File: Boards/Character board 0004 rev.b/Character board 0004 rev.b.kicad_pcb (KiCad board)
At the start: 2 copper layers, 166.4 x 186.7 mm, 64 parts, among them J1 card edge, J2 character connector, Q1 2N6125, U1 2.2K, U10 Unused DIP, U11 ULN2003A, U12 ULN2003A, U13 7406, U14 74LS42, U15 LM741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

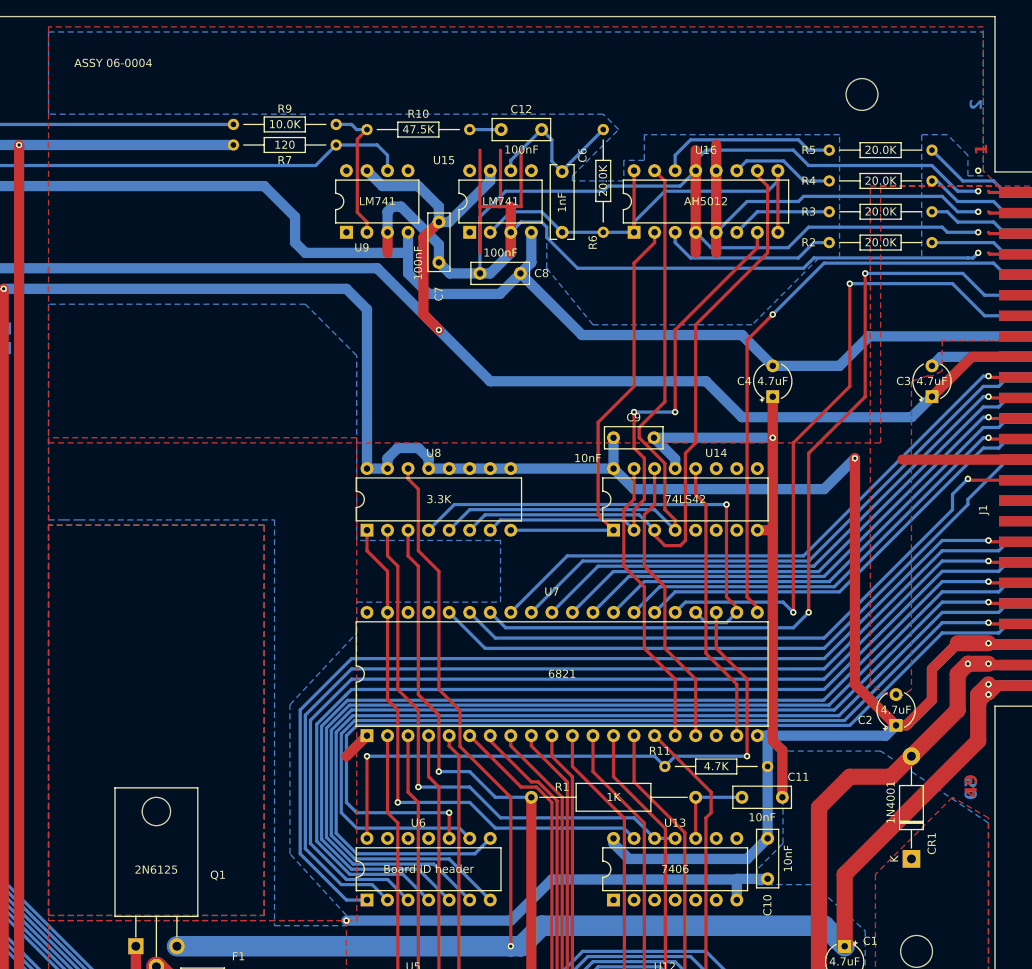
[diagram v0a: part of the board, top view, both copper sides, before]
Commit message: updated boards to have correct logos
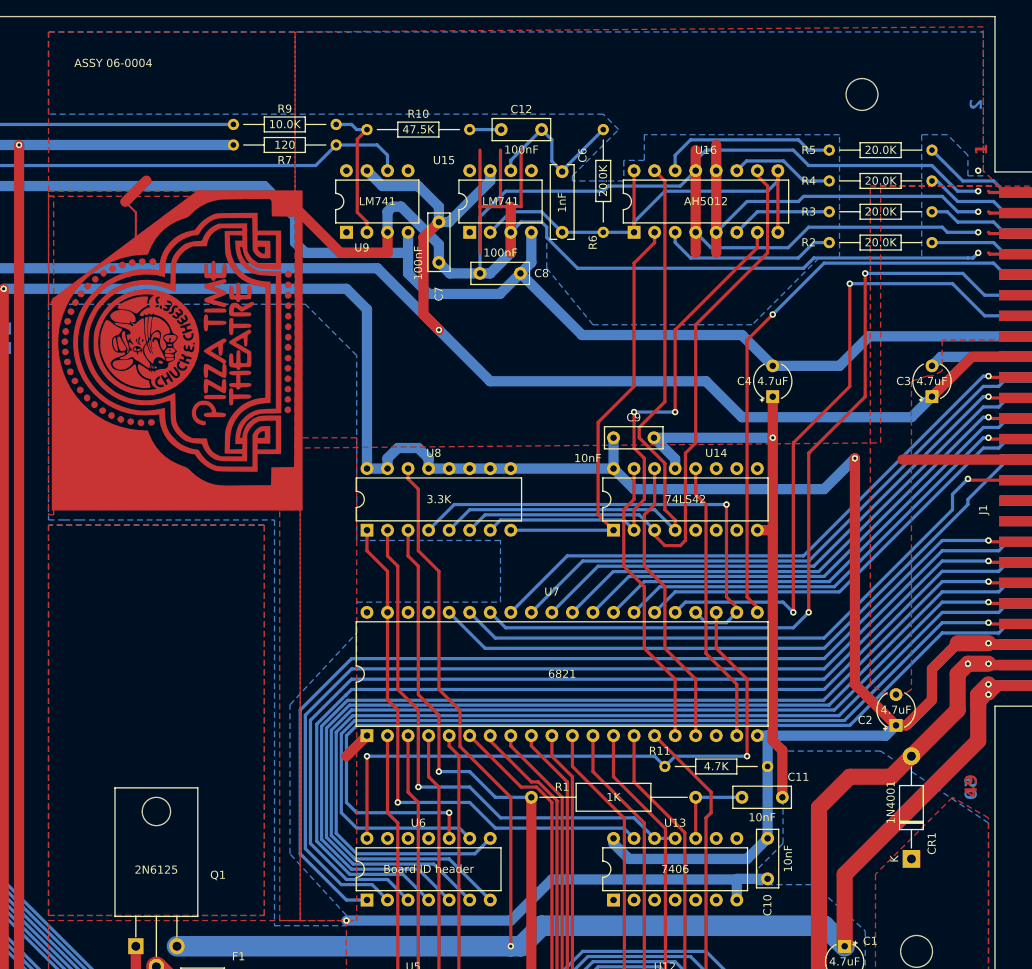
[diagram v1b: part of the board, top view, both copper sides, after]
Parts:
- added G***: LOGO, Evan's parts:PTT white, F.Cu at (83.2, 41.3)
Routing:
- net GND: track 558.6 -> 581.6 mm

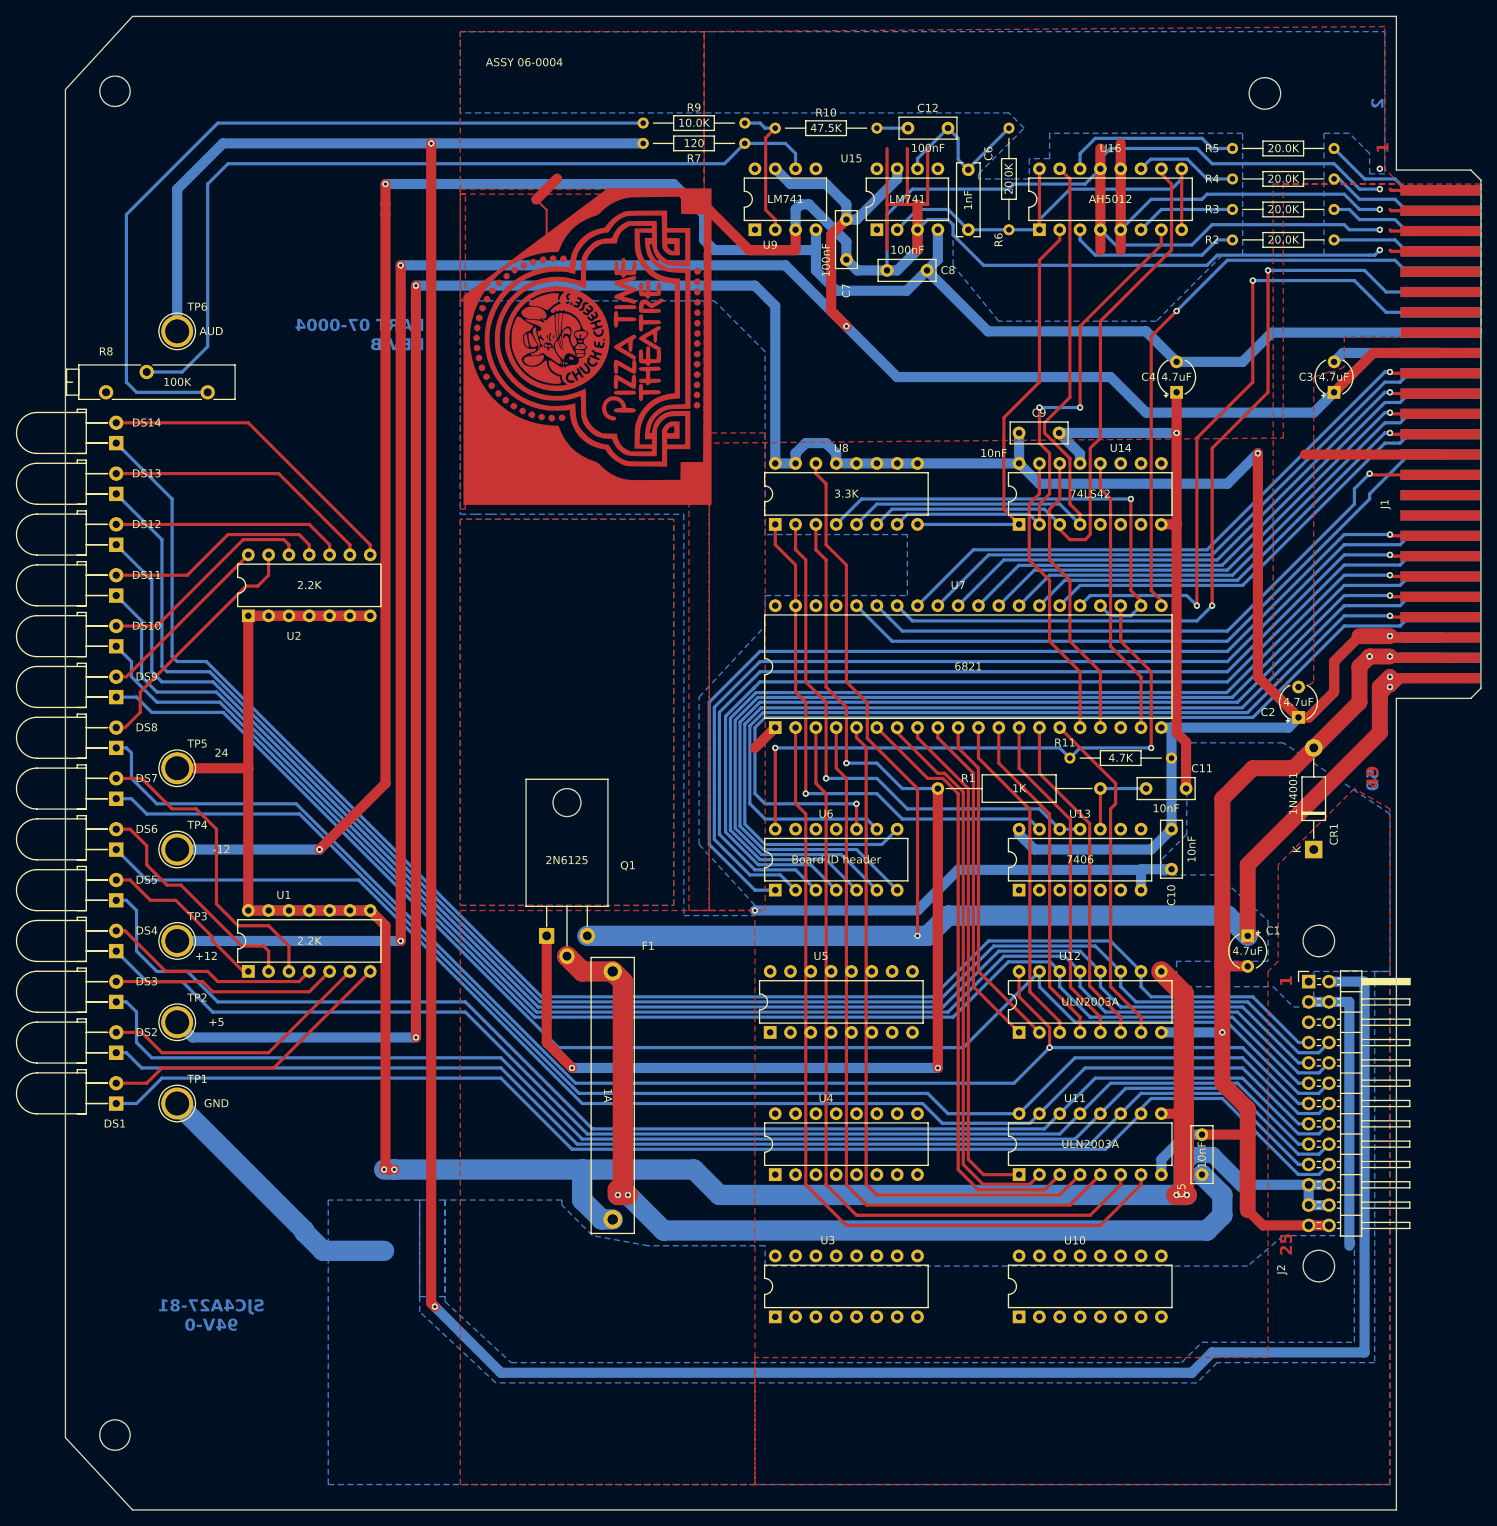
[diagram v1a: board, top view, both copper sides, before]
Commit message: revised LED spacing
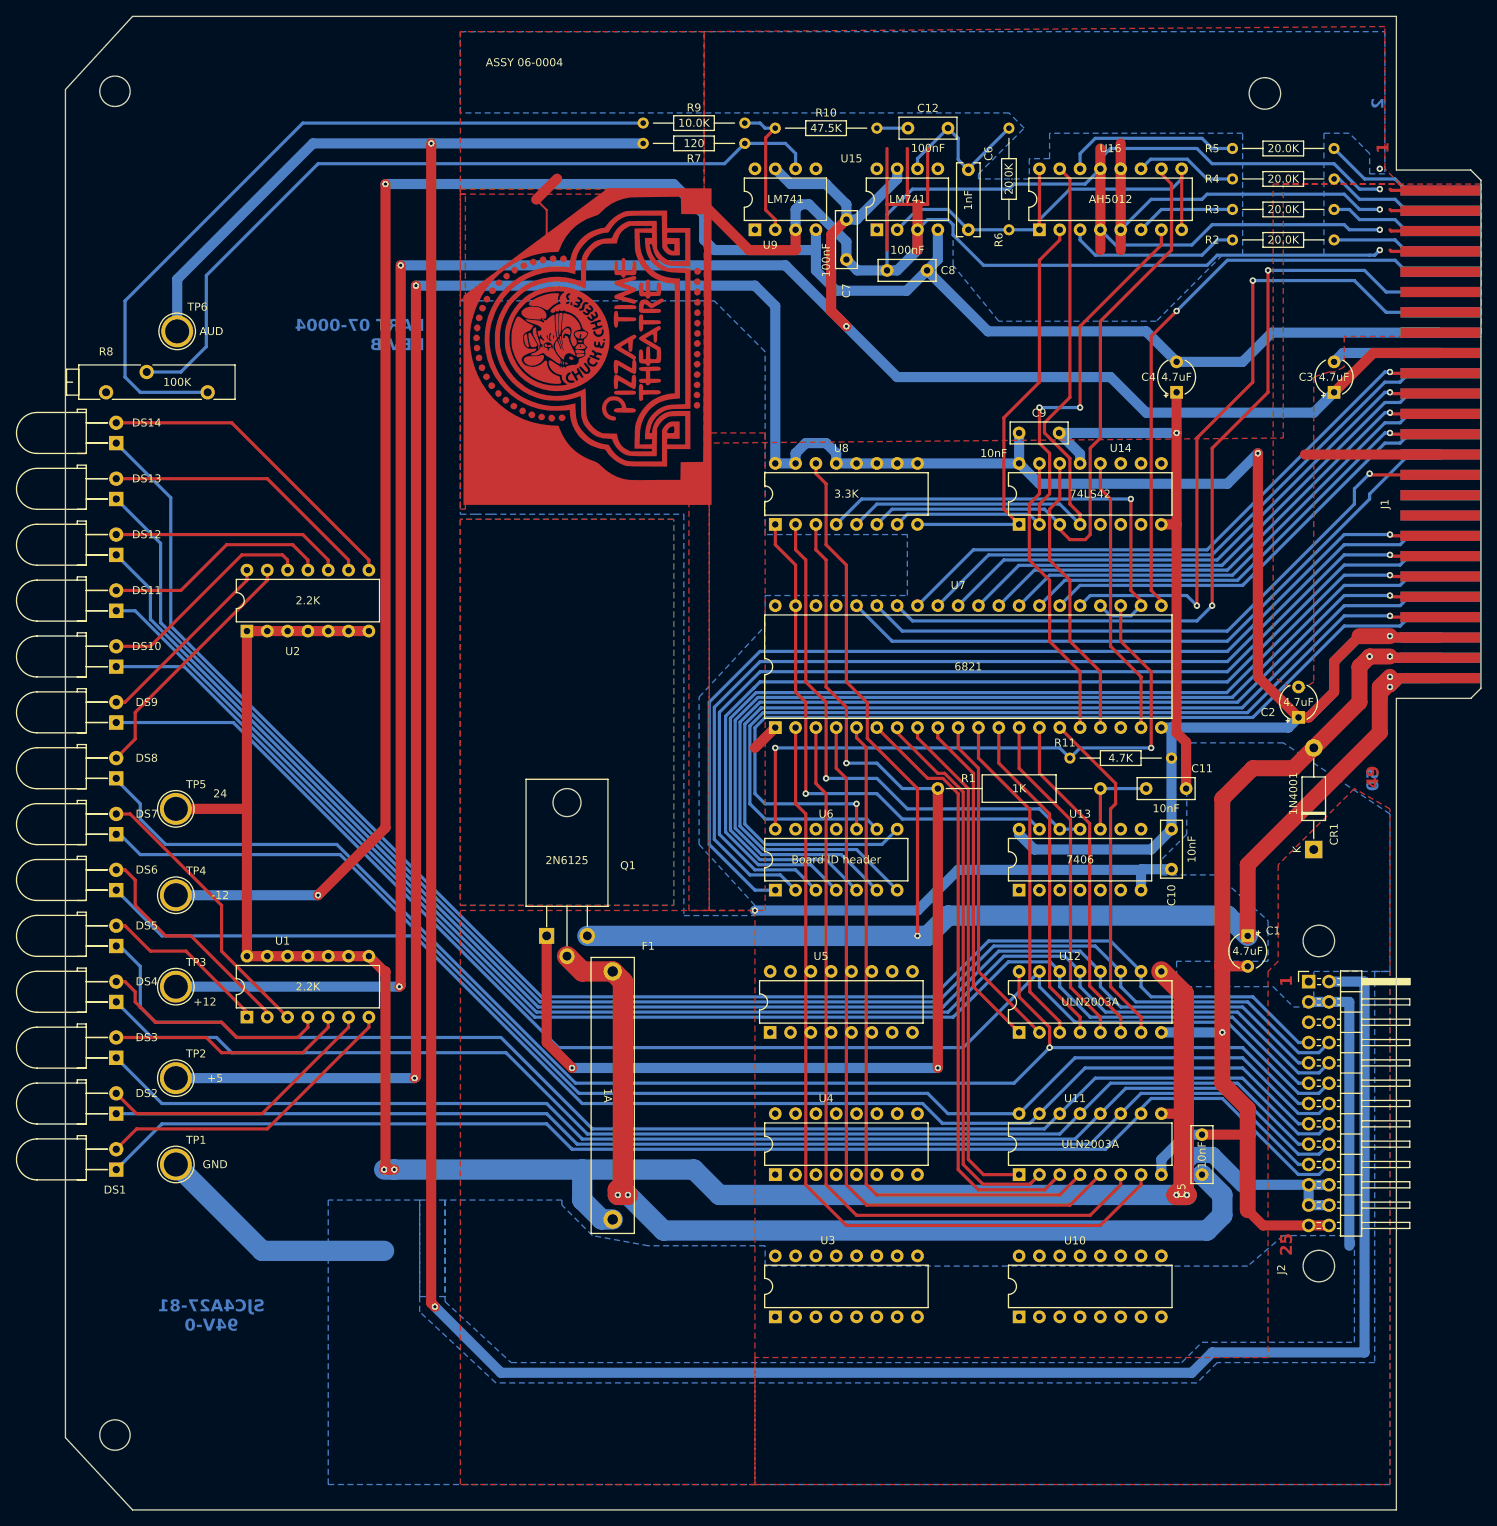
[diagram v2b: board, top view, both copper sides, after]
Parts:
- moved DS1 8.25 mm to (24.3, 141.6)
- moved TP1 7.62 mm to (31.8, 143.5)
- moved DS2 7.62 mm to (24.3, 134.6)
- moved TP2 6.99 mm to (31.8, 132.7)
- moved DS3 6.98 mm to (24.3, 127.6)
- moved DS4 6.35 mm to (24.3, 120.7)
- moved TP3 5.72 mm to (31.8, 121.3)
- moved TP4 5.72 mm to (31.8, 109.9)
- moved U1 5.72 mm to (40.6, 125.1)
- moved DS5 5.72 mm to (24.3, 113.7)
- moved TP5 5.08 mm to (31.8, 99.1)
- moved DS6 5.08 mm to (24.3, 106.7)
- moved DS7 4.44 mm to (24.3, 99.7)
- moved DS8 3.81 mm to (24.3, 92.7)
- moved DS9 3.17 mm to (24.3, 85.7)
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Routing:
- net 24Vout: track 307.0 -> 282.2 mm
- net Net-(R7-Pad2): track 107.3 -> 100.6 mm
- net AUD: track 395.5 -> 388.9 mm
- net Net-(R8-Pad1): track 101.0 -> 94.6 mm
- net 12V: track 290.3 -> 296.0 mm
- net -12V: track 260.6 -> 266.2 mm
- net A2out: track 167.5 -> 162.4 mm
- net B3out: track 189.5 -> 184.5 mm
- net B2out: track 187.8 -> 182.9 mm
- net 5V: track 393.7 -> 397.9 mm
- net B4out: track 197.3 -> 193.5 mm
- net Net-(DS7-A): track 38.9 -> 35.3 mm
- net A1out: track 160.1 -> 156.9 mm
- net GND: track 581.6 -> 578.5 mm
- net A3out: track 164.3 -> 161.7 mm
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
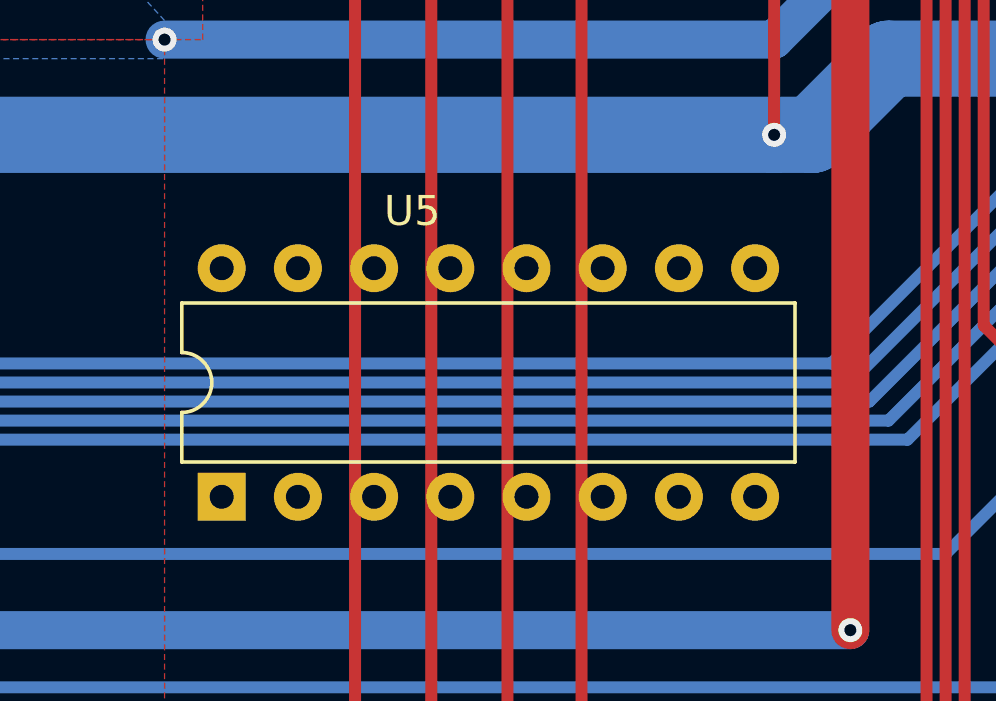
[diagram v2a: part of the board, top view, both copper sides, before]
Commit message: one chip misplaced
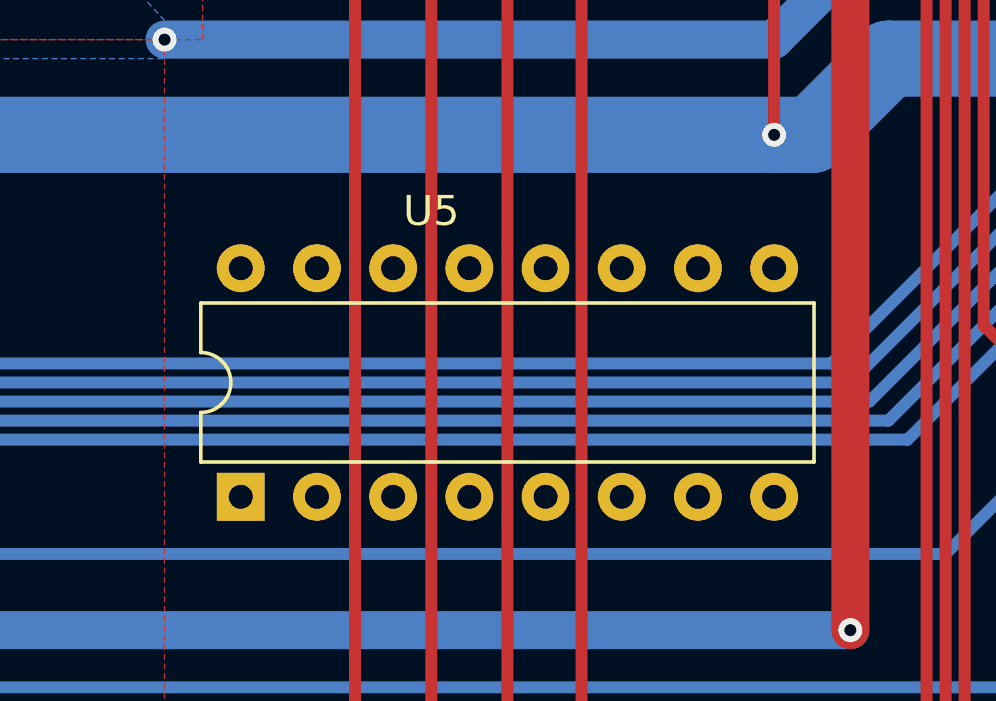
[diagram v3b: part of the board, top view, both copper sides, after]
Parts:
- moved U5 0.64 mm to (106.7, 127.0)
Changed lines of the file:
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@@
   )
   (footprint "Package_DIP:DIP-16_W7.62mm" (layer "F.Cu")
-    (at 106.045 127 90)
+    (at 106.68 127 90)
     (descr "16-lead though-hole mounted DIP package, row spacing 7.62 mm (300 mils)")
     (tags "THT DIP DIL PDIP 2.54mm 7.62mm 300mil")
